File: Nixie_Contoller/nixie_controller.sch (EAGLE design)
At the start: 41 parts, among them IC1 DS1307, IC2 MAX1771ESA, IC3 7805T, J1 CON-SOCJ-2155, Q1 16MHz, T1 IRF644PBF, U1 328P, U2 HU2032-LF, Y2 32.768kHz

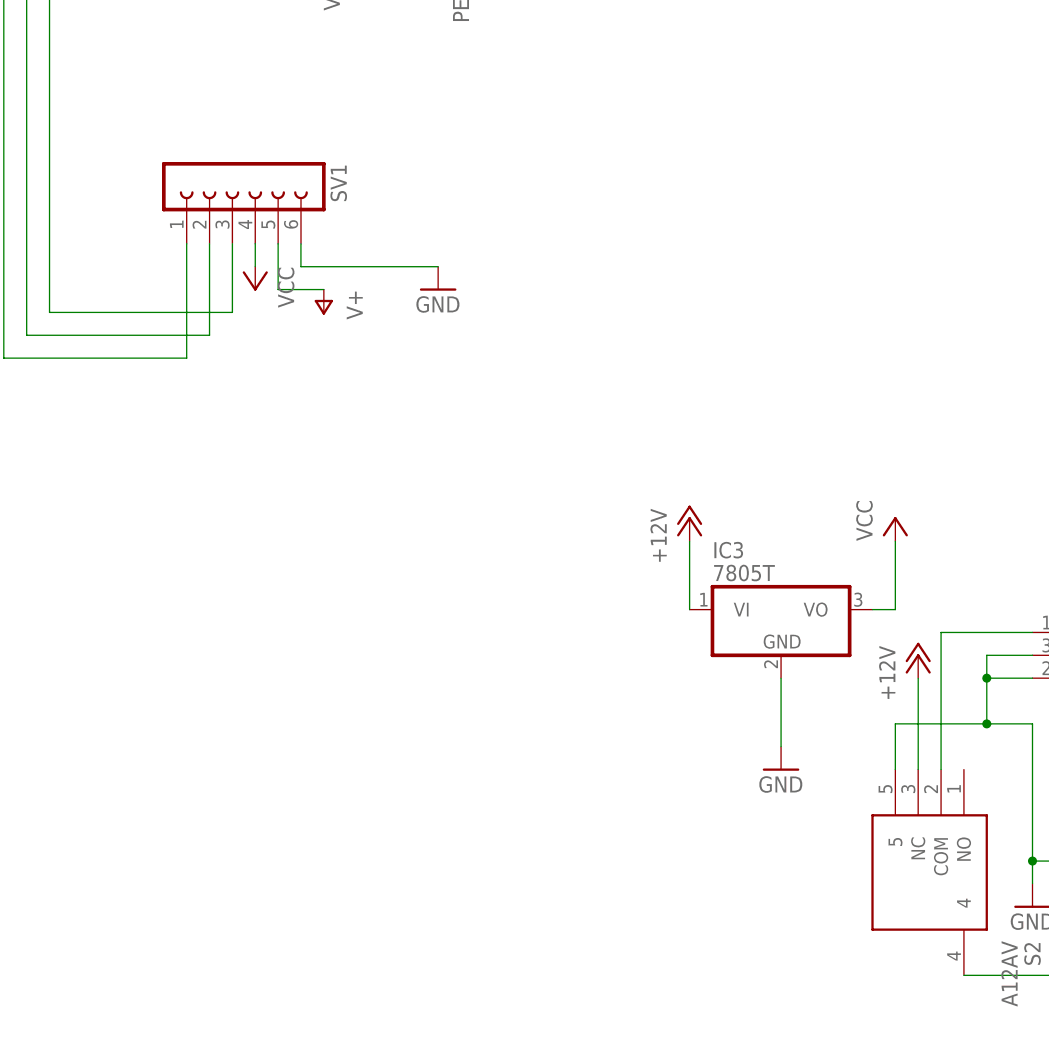
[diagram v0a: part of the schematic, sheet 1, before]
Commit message: Stable PSU, TPIC6b595 working. Release candidate
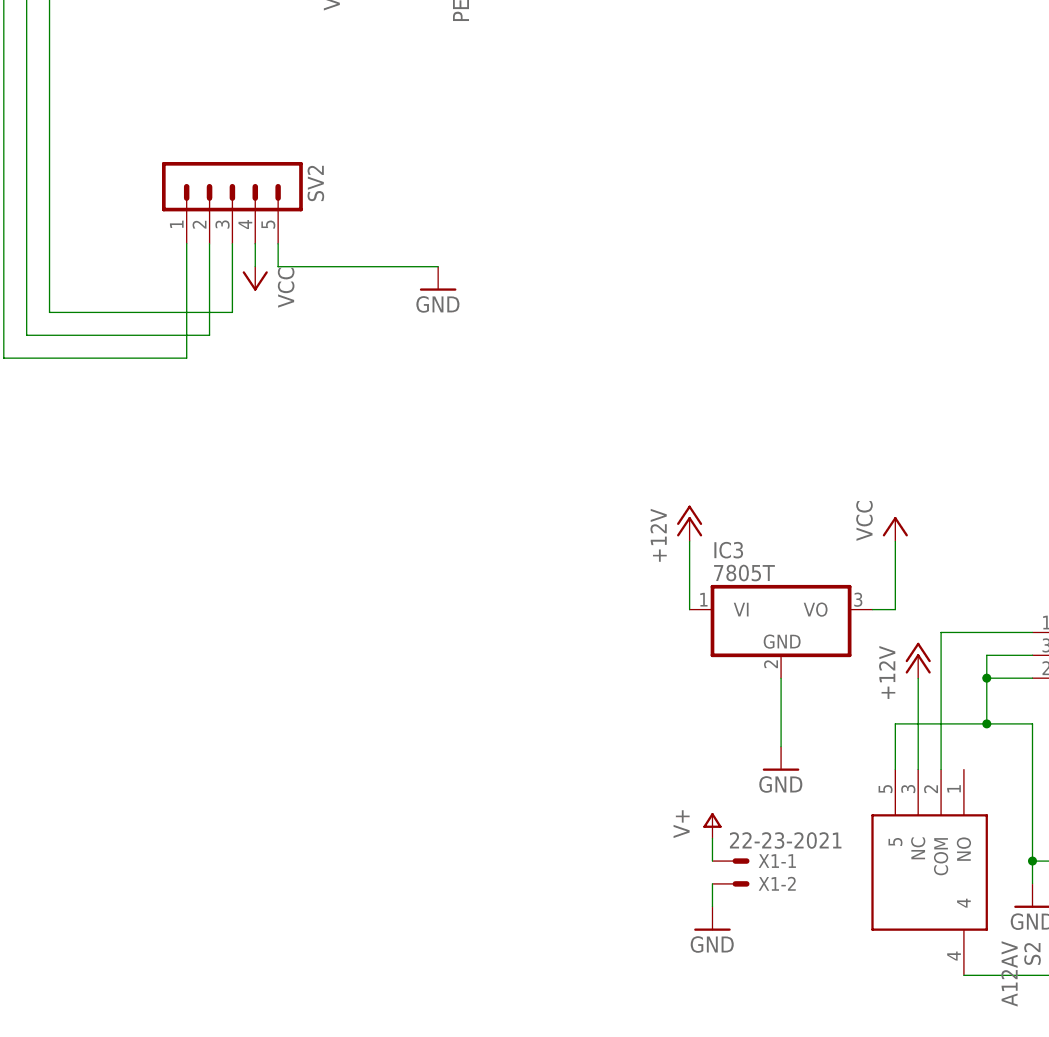
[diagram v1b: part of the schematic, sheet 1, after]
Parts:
- removed SV1: (no value), con-lsta:FE06-1
- added SV2: (no value), con-lstb:MA05-1
- added X1: 22-23-2021, con-molex:22-23-2021
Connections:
- net CLK: now also SV2.1; no longer SV1.1
- net GND: now also SV2.5, X1-2.S; no longer SV1.6
- net N$18: now also SV2.3; no longer SV1.3
- net N$7: now also SV2.2; no longer SV1.2
- net V+: now also X1-1.S; no longer SV1.5
- net VCC: now also SV2.4; no longer SV1.4
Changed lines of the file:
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@@
 <part name="GND6" library="supply1" library_urn="urn:adsk.eagle:library:371" deviceset="GND" device=""/>
 <part name="GND7" library="supply1" library_urn="urn:adsk.eagle:library:371" deviceset="GND" device=""/>
-<part name="SV1" library="con-lsta" library_urn="urn:adsk.eagle:library:161" deviceset="FE06-1" device="" package3d_urn="urn:adsk.eagle:package:8191/1"/>
 <part name="P+9" library="supply1" library_urn="urn:adsk.eagle:library:371" deviceset="VCC" device=""/>
-<part name="P+10" library="supply1" library_urn="urn:adsk.eagle:library:371" deviceset="V+" device=""/>
 <part name="GND8" library="supply1" library_urn="urn:adsk.eagle:library:371" deviceset="GND" device=""/>
 <part name="C3" library="rcl" library_urn="urn:adsk.eagle:library:334" deviceset="C-US" device="050-030X075" package3d_urn="urn:adsk.eagle:package:23640/1" value=".01μf"/>
@@
 <part name="GND19" library="supply1" library_urn="urn:adsk.eagle:library:371" deviceset="GND" device=""/>
 <part name="GND20" library="supply1" library_urn="urn:adsk.eagle:library:371" deviceset="GND" device=""/>
+<part name="SV2" library="con-lstb" library_urn="urn:adsk.eagle:library:162" deviceset="MA05-1" device="" package3d_urn="urn:adsk.eagle:package:8332/1"/>
+<part name="X1" library="con-molex" library_urn="urn:adsk.eagle:library:165" deviceset="22-23-2021" device="" package3d_urn="urn:adsk.eagle:package:8078633/1"/>
+<part name="P+10" library="supply1" library_urn="urn:adsk.eagle:library:371" deviceset="V+" device=""/>
+<part name="GND14" library="supply1" library_urn="urn:adsk.eagle:library:371" deviceset="GND" device=""/>
 </parts>
 <sheets>
@@
 <attribute name="VALUE" x="185.42" y="99.06" size="1.778" layer="96"/>
 </instance>
-<instance part="SV1" gate="G$1" x="165.1" y="114.3" smashed="yes" rot="R270" grouprefs="DISPLAY_CONNECTION">
-<attribute name="VALUE" x="154.94" y="115.57" size="1.778" layer="96" rot="R270"/>
-<attribute name="NAME" x="176.022" y="115.57" size="1.778" layer="95" rot="R270"/>
-</instance>
 <instance part="P+9" gate="VCC" x="167.64" y="101.6" smashed="yes" rot="R180" grouprefs="DISPLAY_CONNECTION">
 <attribute name="VALUE" x="170.18" y="104.14" size="1.778" layer="96" rot="R270"/>
-</instance>
-<instance part="P+10" gate="1" x="175.26" y="99.06" smashed="yes" rot="R180" grouprefs="DISPLAY_CONNECTION">
-<attribute name="VALUE" x="177.8" y="101.6" size="1.778" layer="96" rot="R270"/>
 </instance>
 <instance part="GND8" gate="1" x="175.26" y="170.18" smashed="yes" grouprefs="ENCODER">
@@
 <attribute name="NAME" x="218.44" y="71.755" size="1.778" layer="95"/>
 <attribute name="VALUE" x="218.44" y="69.215" size="1.778" layer="96"/>
+</instance>
+<instance part="SV2" gate="G$1" x="165.1" y="114.3" smashed="yes" rot="R270">
+<attribute name="VALUE" x="154.94" y="115.57" size="1.778" layer="96" rot="R270"/>
+<attribute name="NAME" x="173.482" y="115.57" size="1.778" layer="95" rot="R270"/>
+</instance>
+<instance part="X1" gate="-1" x="220.98" y="38.1" smashed="yes">
+<attribute name="NAME" x="223.52" y="37.338" size="1.524" layer="95"/>
+<attribute name="VALUE" x="220.218" y="39.497" size="1.778" layer="96"/>
+</instance>
+<instance part="X1" gate="-2" x="220.98" y="35.56" smashed="yes">
+<attribute name="NAME" x="223.52" y="34.798" size="1.524" layer="95"/>
+</instance>
+<instance part="P+10" gate="1" x="218.44" y="43.18" smashed="yes">
+<attribute name="VALUE" x="215.9" y="40.64" size="1.778" layer="96" rot="R90"/>
+</instance>
+<instance part="GND14" gate="1" x="218.44" y="30.48" smashed="yes">
+<attribute name="VALUE" x="215.9" y="27.94" size="1.778" layer="96"/>
 </instance>
 </instances>
@@
 </segment>
 </net>
-<net name="GND" class="0">
+<net name="GND" class="1">
 <segment>
 <pinref part="U2" gate="G$1" pin="-_2"/>
@@
 </segment>
 <segment>
-<pinref part="SV1" gate="G$1" pin="6"/>
 <pinref part="GND7" gate="1" pin="GND"/>
-<wire x1="172.72" y1="106.68" x2="172.72" y2="104.14" width="0.1524" layer="91" grouprefs="DISPLAY_CONNECTION"/>
-<wire x1="172.72" y1="104.14" x2="187.96" y2="104.14" width="0.1524" layer="91" grouprefs="DISPLAY_CONNECTION"/>
+<wire x1="170.18" y1="104.14" x2="187.96" y2="104.14" width="0.1524" layer="91" grouprefs="DISPLAY_CONNECTION"/>
+<pinref part="SV2" gate="G$1" pin="5"/>
+<wire x1="170.18" y1="106.68" x2="170.18" y2="104.14" width="0.1524" layer="91"/>
 </segment>
 <segment>
@@
 <wire x1="185.42" y1="144.78" x2="185.42" y2="149.86" width="0.1524" layer="91"/>
 </segment>
+<segment>
+<pinref part="X1" gate="-2" pin="S"/>
+<pinref part="GND14" gate="1" pin="GND"/>
+<wire x1="218.44" y1="35.56" x2="218.44" y2="33.02" width="0.1524" layer="91"/>
+</segment>
 </net>
 <net name="VCC" class="0">
@@
 </segment>
 <segment>
-<pinref part="SV1" gate="G$1" pin="4"/>
 <pinref part="P+9" gate="VCC" pin="VCC"/>
 <wire x1="167.64" y1="106.68" x2="167.64" y2="104.14" width="0.1524" layer="91" grouprefs="DISPLAY_CONNECTION"/>
+<pinref part="SV2" gate="G$1" pin="4"/>
 </segment>
 <segment>
@@
 </segment>
 </net>
-<net name="V+" class="0">
-<segment>
-<pinref part="SV1" gate="G$1" pin="5"/>
-<pinref part="P+10" gate="1" pin="V+"/>
-<wire x1="170.18" y1="106.68" x2="170.18" y2="101.6" width="0.1524" layer="91" grouprefs="DISPLAY_CONNECTION"/>
-<wire x1="170.18" y1="101.6" x2="175.26" y2="101.6" width="0.1524" layer="91" grouprefs="DISPLAY_CONNECTION"/>
-</segment>
-</net>
 <net name="CLK" class="0">
 <segment>
@@
 <wire x1="106.68" y1="149.86" x2="139.7" y2="149.86" width="0.1524" layer="91"/>
 <wire x1="139.7" y1="149.86" x2="139.7" y2="93.98" width="0.1524" layer="91"/>
-<pinref part="SV1" gate="G$1" pin="1"/>
 <wire x1="160.02" y1="93.98" x2="160.02" y2="106.68" width="0.1524" layer="91" grouprefs="DISPLAY_CONNECTION"/>
 <wire x1="139.7" y1="93.98" x2="160.02" y2="93.98" width="0.1524" layer="91"/>
+<pinref part="SV2" gate="G$1" pin="1"/>
 </segment>
 </net>
@@
 <wire x1="106.68" y1="160.02" x2="142.24" y2="160.02" width="0.1524" layer="91"/>
 <wire x1="142.24" y1="160.02" x2="142.24" y2="96.52" width="0.1524" layer="91"/>
-<pinref part="SV1" gate="G$1" pin="2"/>
 <wire x1="162.56" y1="106.68" x2="162.56" y2="96.52" width="0.1524" layer="91"/>
 <wire x1="162.56" y1="96.52" x2="142.24" y2="96.52" width="0.1524" layer="91"/>
+<pinref part="SV2" gate="G$1" pin="2"/>
 </segment>
 </net>
@@
 <net name="N$18" class="0">
 <segment>
-<pinref part="SV1" gate="G$1" pin="3"/>
 <wire x1="165.1" y1="99.06" x2="165.1" y2="106.68" width="0.1524" layer="91" grouprefs="DISPLAY_CONNECTION"/>
 <pinref part="U1" gate="U1" pin="PB3(MOSI/OC2)"/>
@@
 <wire x1="165.1" y1="99.06" x2="144.78" y2="99.06" width="0.1524" layer="91"/>
 <wire x1="144.78" y1="99.06" x2="144.78" y2="152.4" width="0.1524" layer="91"/>
+<pinref part="SV2" gate="G$1" pin="3"/>
 </segment>
 </net>
@@
 <pinref part="S2" gate="G$1" pin="COM"/>
 <wire x1="243.84" y1="63.5" x2="243.84" y2="48.26" width="0.1524" layer="91"/>
+</segment>
+</net>
+<net name="V+" class="0">
+<segment>
+<pinref part="P+10" gate="1" pin="V+"/>
+<pinref part="X1" gate="-1" pin="S"/>
+<wire x1="218.44" y1="40.64" x2="218.44" y2="38.1" width="0.1524" layer="91"/>
 </segment>
 </net>
@@
 </segment>
 </net>
-<net name="GND" class="0">
+<net name="GND" class="1">
 <segment>
 <wire x1="99.06" y1="109.22" x2="50.8" y2="109.22" width="0.1524" layer="91"/>
